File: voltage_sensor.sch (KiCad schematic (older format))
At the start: 22 parts, among them K1 REF, P1 Input, P2 CONN_4, P3 CONN_2, U1 REF5020, U2 LT6011, U3 ADUM5401, U4 MCP3550

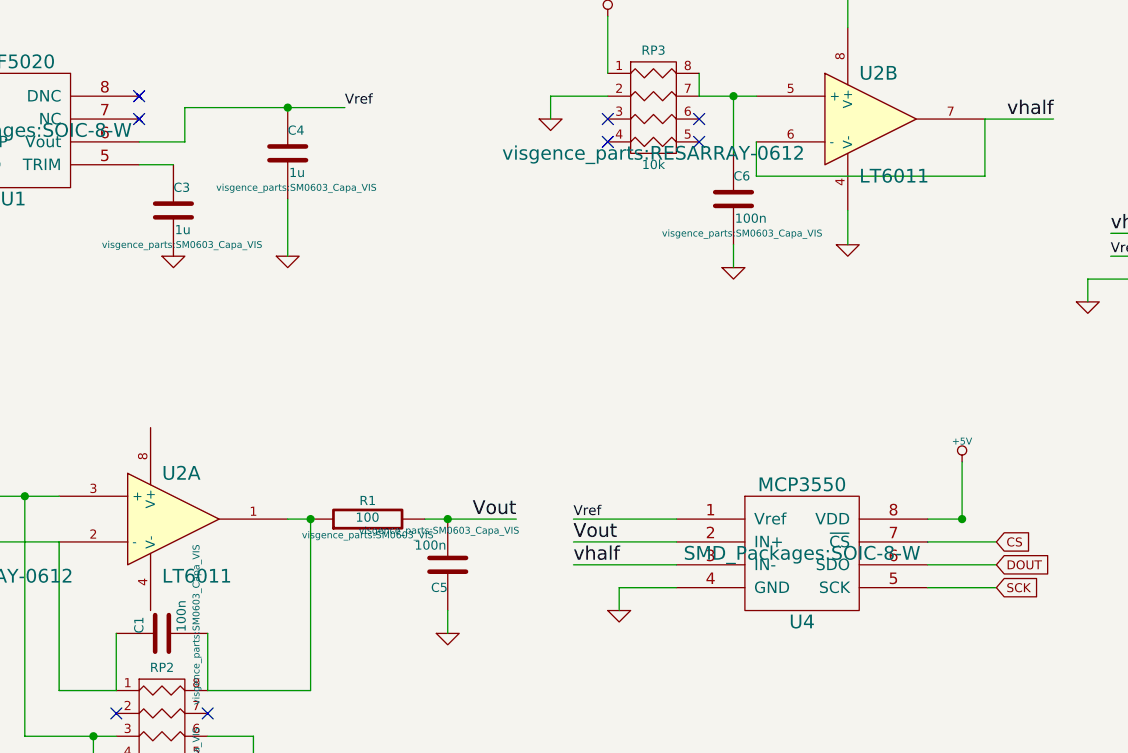
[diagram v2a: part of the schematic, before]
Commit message: Changed Opamp to chopper
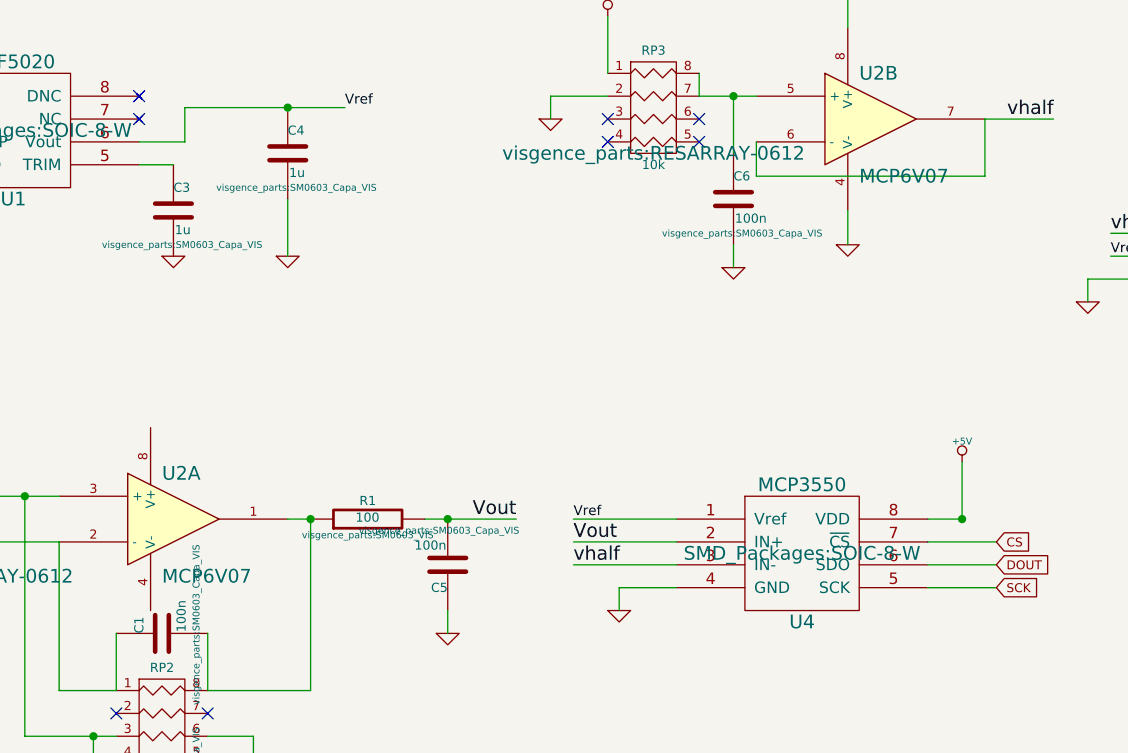
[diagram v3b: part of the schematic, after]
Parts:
- U2: value LT6011 -> MCP6V07
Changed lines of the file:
@@
 EESchema Schematic File Version 2
+LIBS:74xx
+LIBS:adc-dac
+LIBS:analog_switches
+LIBS:atmel
+LIBS:audio
+LIBS:cmos4000
+LIBS:conn
+LIBS:contrib
+LIBS:cypress
+LIBS:device
+LIBS:digital-audio
+LIBS:display
+LIBS:dsp
+LIBS:intel
+LIBS:interface
+LIBS:linear
+LIBS:memory
+LIBS:microchip
+LIBS:microcontrollers
+LIBS:motorola
+LIBS:opto
+LIBS:philips
 LIBS:power
-LIBS:device
+LIBS:regul
+LIBS:siliconi
+LIBS:special
+LIBS:texas
 LIBS:transistors
-LIBS:conn
-LIBS:linear
-LIBS:regul
-LIBS:74xx
-LIBS:cmos4000
-LIBS:adc-dac
-LIBS:memory
-LIBS:xilinx
-LIBS:special
-LIBS:microcontrollers
-LIBS:dsp
-LIBS:microchip
-LIBS:analog_switches
-LIBS:motorola
-LIBS:texas
-LIBS:intel
-LIBS:audio
-LIBS:interface
-LIBS:digital-audio
-LIBS:philips
-LIBS:display
-LIBS:cypress
-LIBS:siliconi
-LIBS:opto
-LIBS:atmel
-LIBS:contrib
 LIBS:valves
 LIBS:visgence_parts
+LIBS:xilinx
 LIBS:voltage_sensor-cache
 EELAYER 24 0
@@
 P 6600 3050
 F 0 "U2" H 6550 3250 60  0000 L CNN
-F 1 "LT6011" H 6550 2800 60  0000 L CNN
+F 1 "MCP6V07" H 6550 2800 60  0000 L CNN
 F 2 "SMD_Packages:SOIC-8-W" H 6600 3050 60  0001 C CNN
 F 3 "" H 6600 3050 60  0000 C CNN
@@
 P 3550 4800
 F 0 "U2" H 3500 5000 60  0000 L CNN
-F 1 "LT6011" H 3500 4550 60  0000 L CNN
+F 1 "MCP6V07" H 3500 4550 60  0000 L CNN
 F 2 "SMD_Packages:SOIC-8-W" H 3550 4800 60  0001 C CNN
 F 3 "" H 3550 4800 60  0000 C CNN
